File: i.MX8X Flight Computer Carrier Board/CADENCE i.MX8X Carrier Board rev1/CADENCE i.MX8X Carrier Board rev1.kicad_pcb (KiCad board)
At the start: 6 copper layers, 167.7 x 85 mm, 430 parts, among them CN1 DF11-16DP-2DSA(08), CN2 DF11-16DP-2DSA(08), CN3 DF11-16DP-2DSA(08), CN4 DF11-16DP-2DSA(08), J1 BTH-070-02-L-D-A, J10 Conn_01x04, J11 Conn_01x04, J16 Conn_01x04, J17 Conn_01x04, J2 USB_C_Receptacle_USB2.0_16P, J21 Conn_02x02_Odd_Even, J3 USB_A, J4 Conn_Coaxial, J5 USB_C_Receptacle_USB2.0_16P, J6 Conn_01x01, J7 Conn_01x08, J8 Conn_02x26_Odd_Even, J9 Conn_02x26_Odd_Even, Q1 IRLML6401, Q2 BSS138, Q3 BSS138, SW1 SW_DIP_x01, SW2 KMR221GLFS, SW3 SW_DIP_x04, SW4 SW_DIP_x01, T1 WE-RJ45_7499111121A, T2 WE-RJ45_7499111121A, U1 LT8612, U10 ZDSD04GLGEAG, U11 MR20H40, U12 MR20H40, U13 DP83867IRRGZR, U14 74LVC2G07, U15 USBLC6-2SC6, U16 USBLC6-2SC6, U17 SN65C1168ERGYR, U18 P82B715DR, U19 P82B715DR, U2 LT8612, U20 P82B715DR, U21 INA219AxDCN, U22 Skytraq Orion B16 GPS, U23 RV-3028-C7, U24 LSM6DSO, U25 LIS2MDL, U26 TMP112xxDRL, U27 INA219AxDCN, U28 LP38693MP-ADJ/NOPB, U29 74CBTLV3257BQ, U3 TPS22975, U30 CAT93C66VI-GT3, U31 USBLC6-2SC6, U32 FT2232HL, U33 SN65HVD233, U34 INA219AxDCN, U35 TPS22810DBV, U36 INA219AxDCN, U37 TPS22810DBV, U38 INA219AxDCN, U39 TPS22975, U4 LT3115-1, U40 TXS0101DCKR, U41 TXS0101DCKR, U5 TLV71325PDQNR, U6 TLV71310PDQNR, U7 TLV1704, U8 BD2204GUL-E2, U9 MX25UM51245G, Y1 25MHz, Y2 12MHz

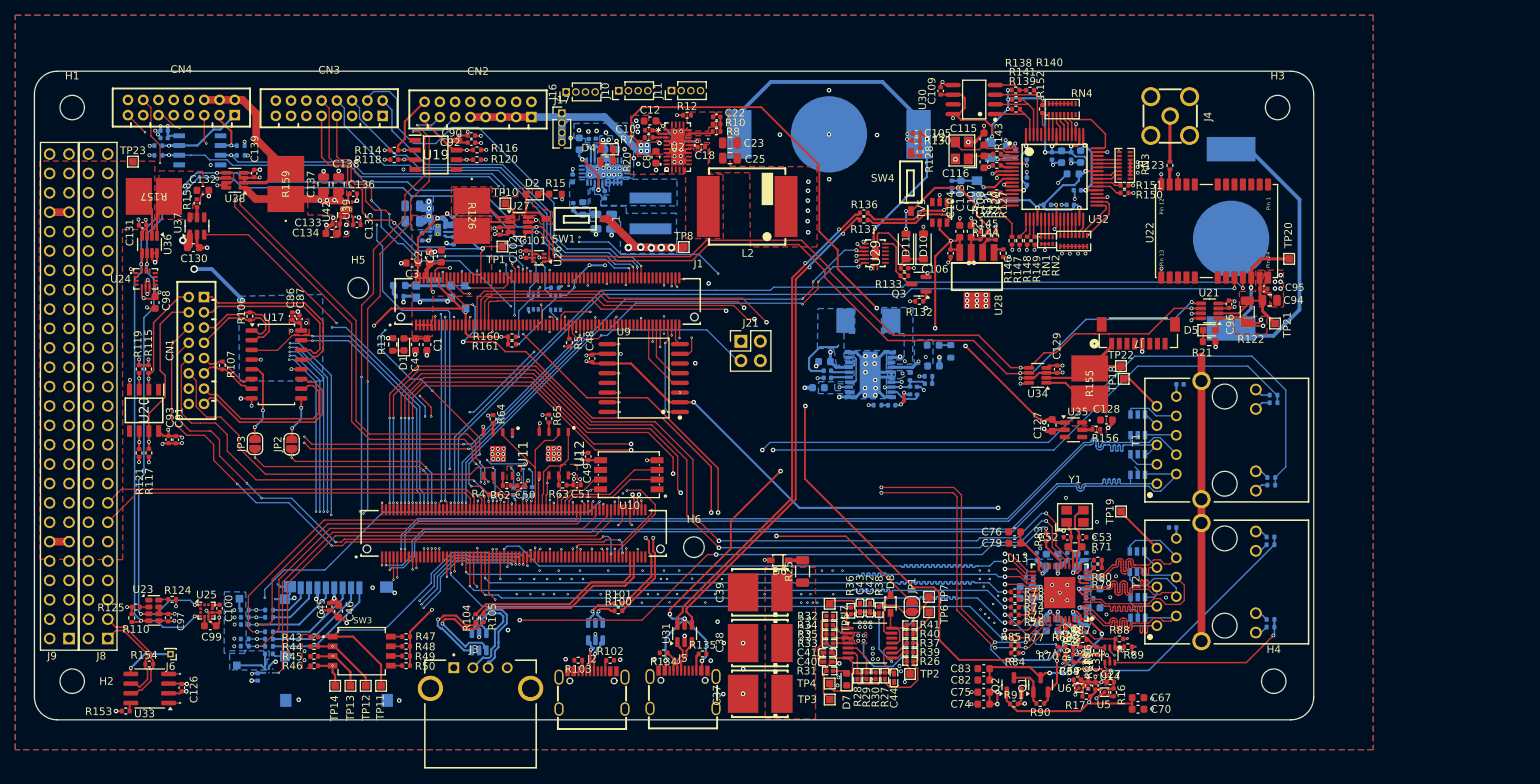
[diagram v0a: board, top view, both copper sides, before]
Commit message: BOM part selection, DRC fixes for traces & shorted vias, fixed power pours mentioned in previous design review
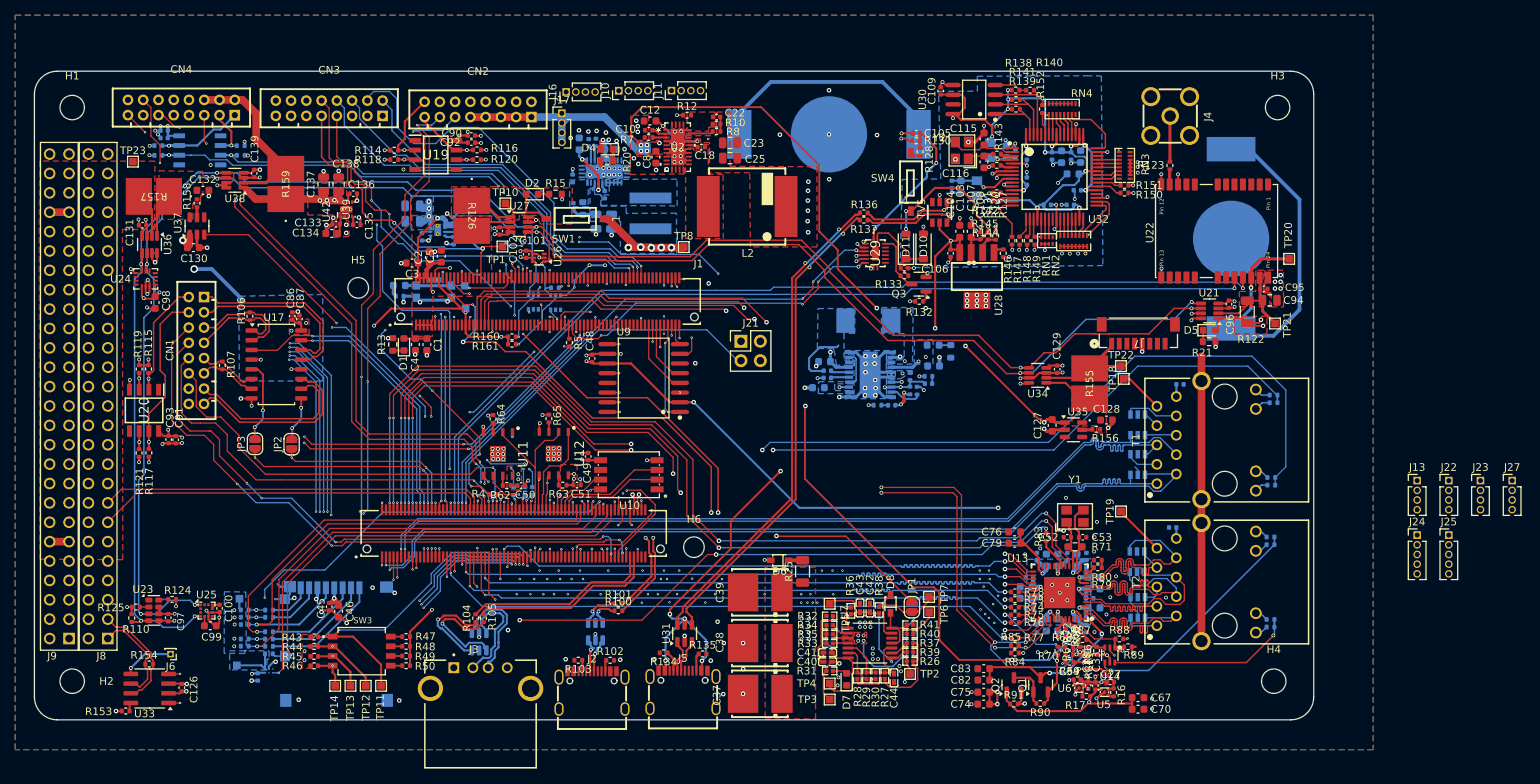
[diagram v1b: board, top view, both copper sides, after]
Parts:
- added J13: Conn_01x04, Connector_PinHeader_1.27mm:PinHeader_1x04_P1.27mm_Vertical, F.Cu at (401.3, 119.5)
- added J22: Conn_01x04, Connector_PinHeader_1.27mm:PinHeader_1x04_P1.27mm_Vertical, F.Cu at (405.5, 119.5)
- added J23: Conn_01x04, Connector_PinHeader_1.27mm:PinHeader_1x04_P1.27mm_Vertical, F.Cu at (409.6, 119.5)
- added J24: Conn_01x05, Connector_PinHeader_1.27mm:PinHeader_1x05_P1.27mm_Vertical, F.Cu at (401.3, 126.7)
- added J25: Conn_01x05, Connector_PinHeader_1.27mm:PinHeader_1x05_P1.27mm_Vertical, F.Cu at (405.5, 126.7)
- added J27: Conn_01x04, Connector_PinHeader_1.27mm:PinHeader_1x04_P1.27mm_Vertical, F.Cu at (413.8, 119.5)
- C29, C30, C35: value 0.1uF -> 100nF
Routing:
- net GND: track 275.1 -> 276.6 mm
- net /FTDI/enable_ftdi: track 19.2 -> 20.2 mm
- added copper zone on B.Cu, net 3V3_FTDI
